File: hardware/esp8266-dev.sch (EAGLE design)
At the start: 14 parts, among them J1 AVR_SPI_PRG_6PTH, X2 PN61729-S

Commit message: generic little wire conversion complete
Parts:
- removed D1, D2: 3.6V, diode:ZENER-DIODEZD-5
- removed JP1: (no value), SparkFun:JUMPER-2PTH
- removed R4: 150, rcl:R-EU_0204/5
- removed X2: PN61729-S, con-berg:PN61729-S
- added C3: 100n, rcl:C-EU025-025X050
- added CON1: USBB-SOCKET, p.peter-connectors:USBB-SOCKET
- added ESP8266: (no value), pinhead:PINHD-2X4
- added F1: PTCPTH, SparkFun:PTCPTH
- added IC1: TBD, v-reg:78LXX
- added R5: 150, rcl:R-EU_0204/7
- added SJ1: (no value), jumper:SJ
- added SW1: (no value), p.peter-passives:SWITCH-DEFAULT_OFF-DEFAULT
- added UART-AVR, UART-ESP: UART-6_PIN, p.peter-connectors:UART-6_PIN
- C1, C2: device rcl:C-EU050-025X075 -> rcl:C-EU025-025X050
- R1, R2, R3: device rcl:R-EU_0204/5 -> rcl:R-EU_0204/7
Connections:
- removed net D-: D2.C, R2.1, R3.1, X2.1
- removed net VCC: C1.2, C2.2, JP1.1, R3.2, R4.2, UC.VCC, X2.4
- new net +3V3: C1.2, C3.2, IC1.OUT, LED1.A, SJ1.2, UART-AVR.VCC, UART-ESP.VCC, UC.VCC
- new net +5V: C2.2, F1.1, IC1.IN, R3.2
- new net N$4: CON1.VBUS, F1.2
- new net N$5: CON1.D-, R2.1, R3.1
- new net N$6: UART-AVR.TX, UART-ESP.TX
- new net N$7: UART-AVR.RX, UART-ESP.RX
- net D+: now also CON1.D+; no longer D1.C, X2.2
- net GND: now also C3.1, CON1.GND, IC1.GND, R5.1, UART-AVR.GND, UART-ESP.GND; no longer D1.A, D2.A, LED1.C, X2.3
- net N$3: now also LED1.C, R5.2; no longer LED1.A, R4.1
- net VCC_HEADER: now also SJ1.1; no longer JP1.2
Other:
- moved on the sheet: C2, LED1, R1, R2, R3

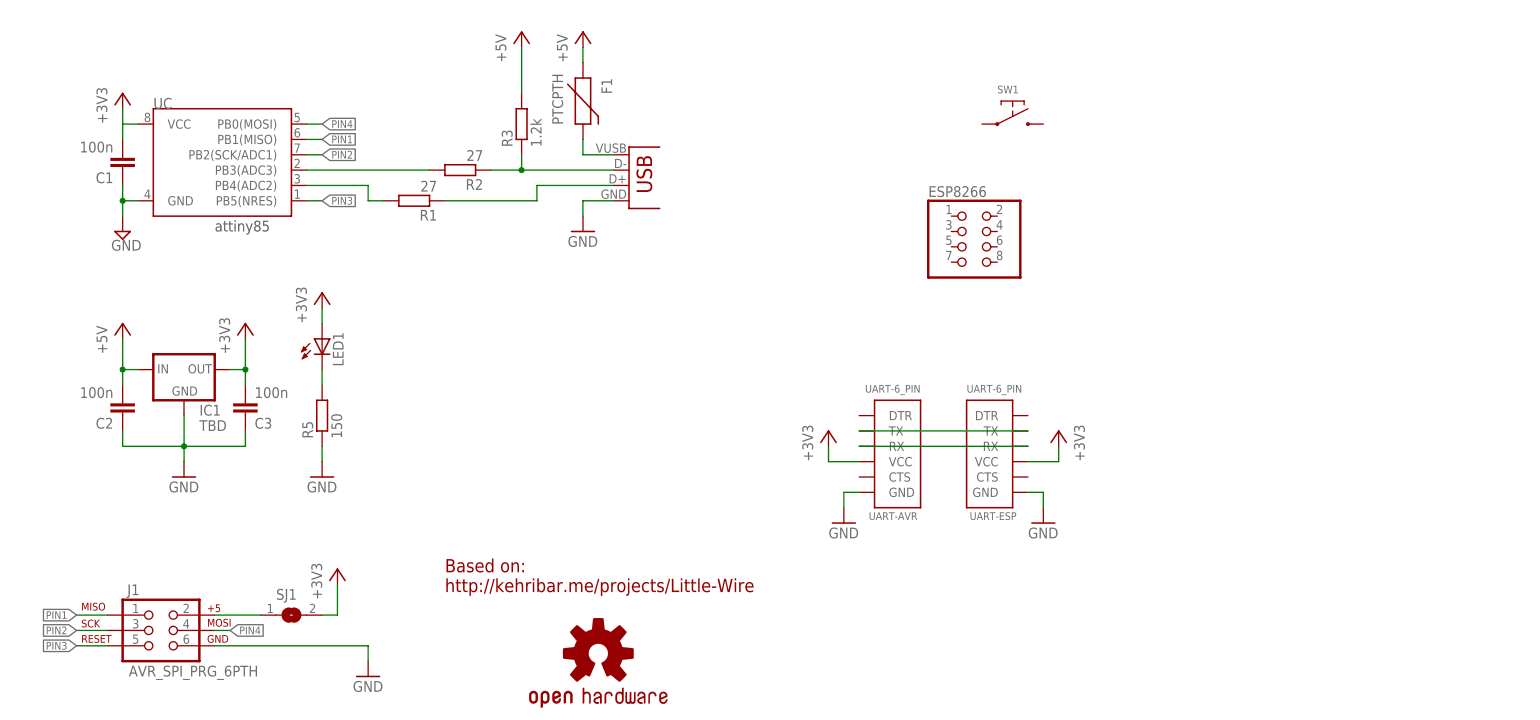
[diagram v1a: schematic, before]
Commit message: Added ESP sub board with proto area
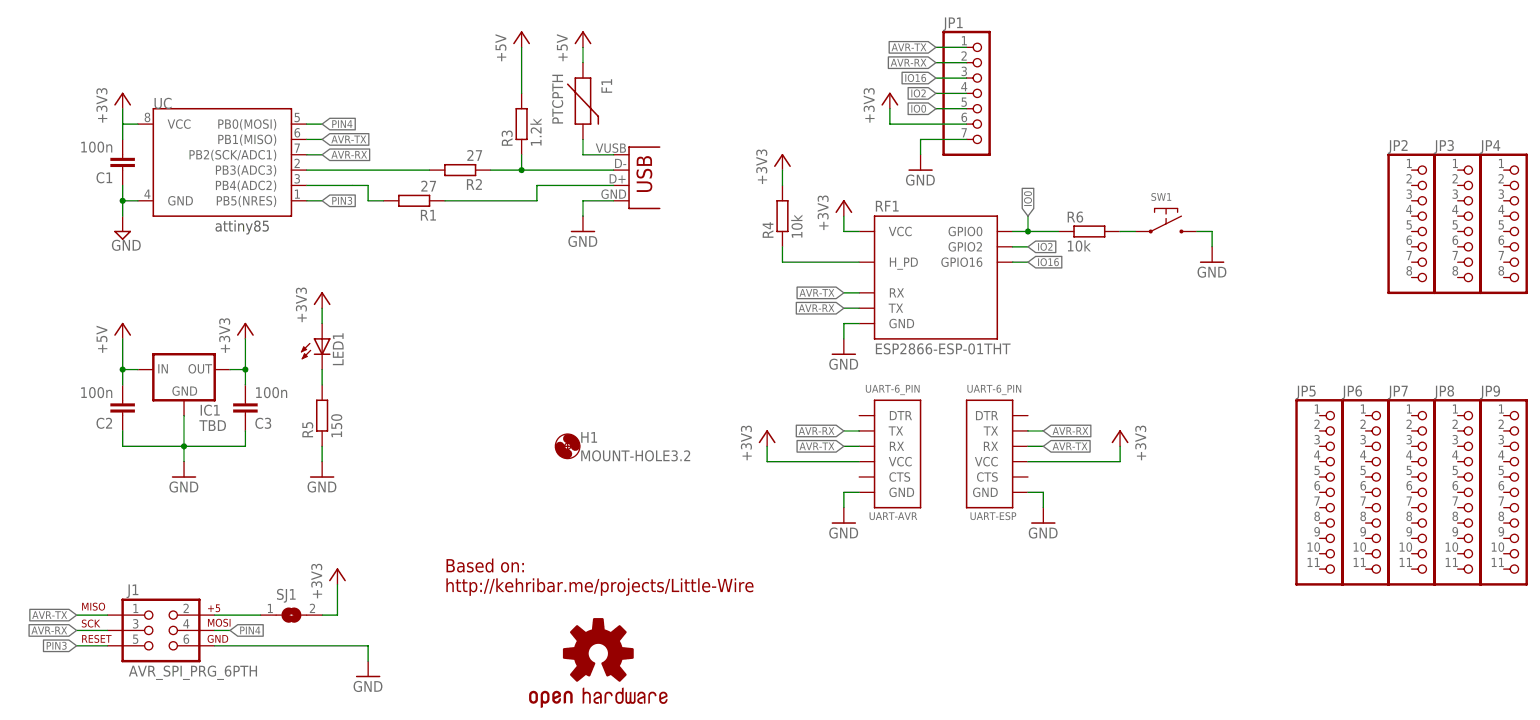
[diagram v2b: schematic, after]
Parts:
- removed ESP8266: (no value), pinhead:PINHD-2X4
- added H1: MOUNT-HOLE3.2, holes:MOUNT-HOLE3.2
- added JP1: (no value), pinhead:PINHD-1X7
- added JP2, JP3, JP4: (no value), pinhead:PINHD-1X8
- added JP5, JP6, JP7, JP8, JP9: (no value), pinhead:PINHD-1X11
- added R4, R6: 10k, rcl:R-EU_0204/7
- added RF1: ESP2866-ESP-01THT, p.peter-periphery:ESP2866-ESP-01THT
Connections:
- removed net N$7: UART-AVR.RX, UART-ESP.RX
- removed net PIN1: J1.1, UC.PB1(MISO)
- removed net PIN2: J1.3, UC.PB2(SCK/ADC1)
- new net AVR-RX: J1.3, JP1.2, RF1.TX, UART-AVR.TX, UART-ESP.TX, UC.PB2(SCK/ADC1)
- new net AVR-TX: J1.1, JP1.1, RF1.RX, UART-AVR.RX, UART-ESP.RX, UC.PB1(MISO)
- new net IO0: JP1.5, R6.1, RF1.GPIO0
- new net IO16: JP1.3, RF1.GPIO16
- new net IO2: JP1.4, RF1.GPIO2
- new net N$8: R6.2, SW1.P$1
- net +3V3: now also JP1.6, R4.2, RF1.VCC
- net GND: now also JP1.7, RF1.GND, SW1.P$2
- net N$6: now also R4.1, RF1.H_PD; no longer UART-AVR.TX, UART-ESP.TX
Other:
- moved on the sheet: SW1

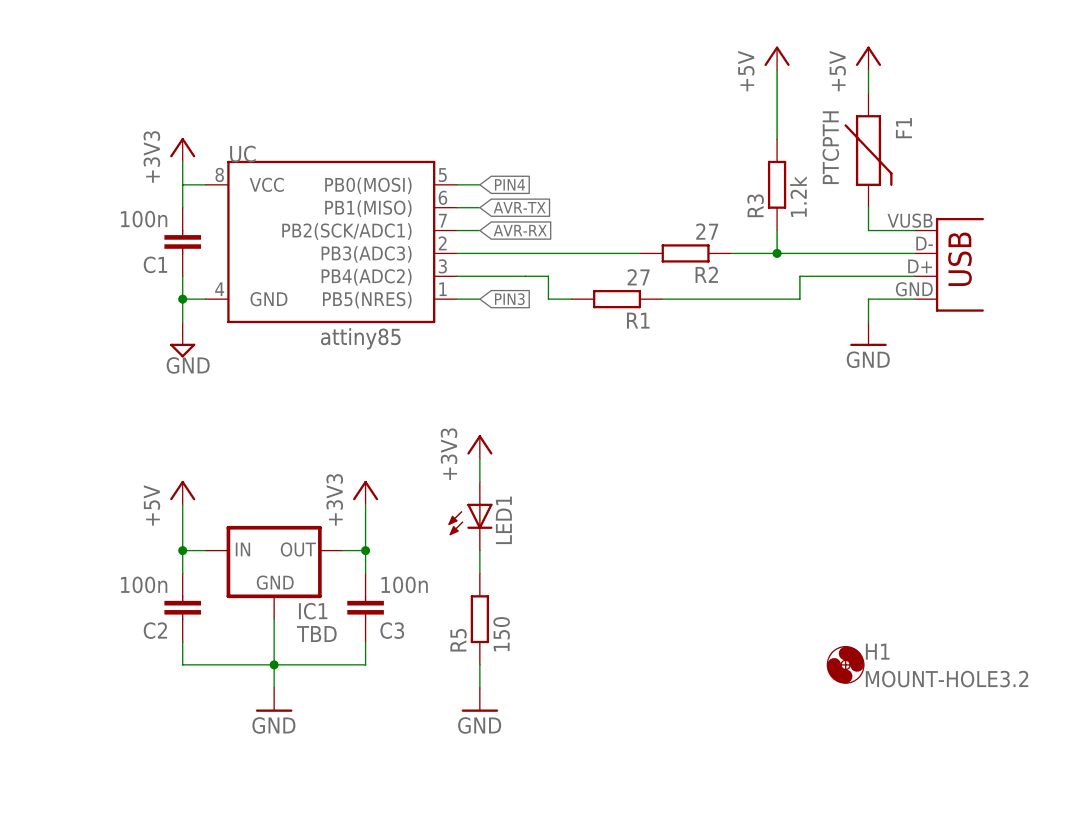
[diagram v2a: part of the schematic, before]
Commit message: changed regulator to 500m suitable version and fuse to smaller footprint
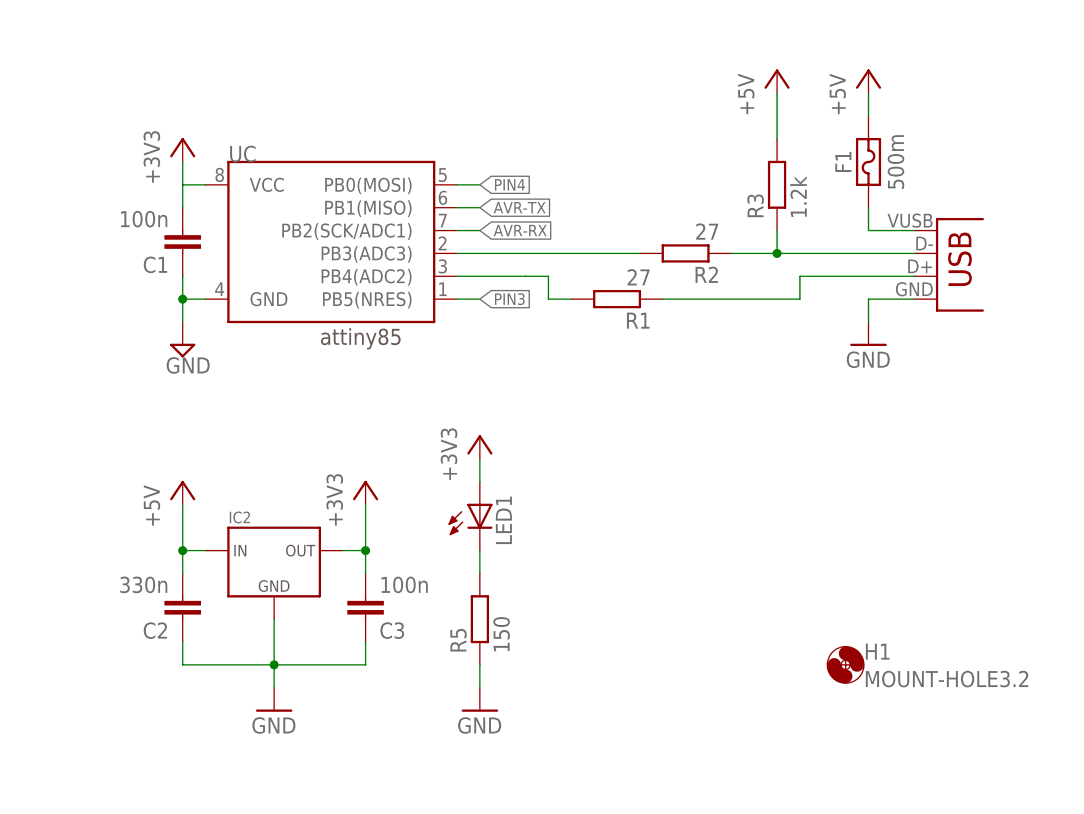
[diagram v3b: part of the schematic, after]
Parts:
- removed IC1: TBD, v-reg:78LXX
- added IC2: (no value), p.peter-regulators:REGULATOR-UA78M33TO220
- C2: value 100n -> 330n
- F1: value PTCPTH -> 500m; device SparkFun:PTCPTH -> p.peter-regulators:FUSETHT-5.1
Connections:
- net +3V3: now also IC2.OUT; no longer IC1.OUT
- net +5V: now also F1.P$2, IC2.IN; no longer F1.1, IC1.IN
- net GND: now also IC2.GND; no longer IC1.GND
- net N$4: now also F1.P$1; no longer F1.2
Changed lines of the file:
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@@
 <layer number="108" name="centerline" color="7" fill="1" visible="no" active="yes"/>
 <layer number="109" name="ref-old" color="11" fill="1" visible="no" active="yes"/>
+<layer number="110" name="fp0" color="7" fill="1" visible="no" active="yes"/>
 <layer number="116" name="Patch_BOT" color="9" fill="4" visible="yes" active="yes"/>
 <layer number="121" name="_tsilk" color="7" fill="1" visible="yes" active="yes"/>
 <layer number="122" name="_bsilk" color="7" fill="1" visible="yes" active="yes"/>
+<layer number="123" name="tTestmark" color="7" fill="1" visible="no" active="yes"/>
+<layer number="124" name="bTestmark" color="7" fill="1" visible="no" active="yes"/>
 <layer number="125" name="_tNames" color="7" fill="1" visible="yes" active="yes"/>
 <layer number="131" name="prix" color="7" fill="1" visible="no" active="yes"/>
@@
 <part name="U$1" library="SparkFun" deviceset="OSHW-LOGO" device="S"/>
 <part name="LED1" library="led" deviceset="LED" device="3MM"/>
-<part name="IC1" library="v-reg" deviceset="78LXX" device="" value="TBD"/>
 <part name="P+1" library="supply1" deviceset="+5V" device=""/>
 <part name="+3V1" library="supply1" deviceset="+3V3" device=""/>
@@
 <part name="+3V4" library="supply1" deviceset="+3V3" device=""/>
 <part name="P+3" library="supply1" deviceset="+5V" device=""/>
-<part name="C2" library="rcl" deviceset="C-EU" device="025-025X050" value="100n"/>
+<part name="C2" library="rcl" deviceset="C-EU" device="025-025X050" value="330n"/>
 <part name="C3" library="rcl" deviceset="C-EU" device="025-025X050" value="100n"/>
 <part name="UART-AVR" library="p.peter-connectors" deviceset="UART-6_PIN" device=""/>
@@
 <part name="+3V6" library="supply1" deviceset="+3V3" device=""/>
 <part name="SW1" library="p.peter-passives" deviceset="SWITCH-DEFAULT_OFF" device="-DEFAULT"/>
-<part name="F1" library="SparkFun" deviceset="PTC" device="PTH"/>
 <part name="SJ1" library="jumper" deviceset="SJ" device=""/>
 <part name="CON1" library="p.peter-connectors" deviceset="USB" device="B-SOCKET"/>
@@
 <part name="GND9" library="supply1" deviceset="GND" device=""/>
 <part name="+3V9" library="supply1" deviceset="+3V3" device=""/>
+<part name="IC2" library="p.peter-regulators" deviceset="REGULATOR-UA78M33" device="TO220"/>
+<part name="F1" library="p.peter-regulators" deviceset="FUSE" device="THT-5.1" value="500m"/>
 </parts>
 <sheets>
@@
 <instance part="U$1" gate="G$1" x="111.76" y="13.97"/>
 <instance part="LED1" gate="G$1" x="66.04" y="66.04"/>
-<instance part="IC1" gate="1" x="43.18" y="60.96"/>
-<instance part="P+1" gate="1" x="109.22" y="116.84"/>
+<instance part="P+1" gate="1" x="109.22" y="114.3"/>
 <instance part="+3V1" gate="G$1" x="53.34" y="68.58"/>
 <instance part="GND1" gate="1" x="43.18" y="43.18"/>
@@
 <instance part="+3V2" gate="G$1" x="66.04" y="73.66"/>
 <instance part="R5" gate="G$1" x="66.04" y="53.34" rot="R90"/>
-<instance part="P+2" gate="1" x="99.06" y="116.84"/>
+<instance part="P+2" gate="1" x="99.06" y="114.3"/>
 <instance part="GND3" gate="1" x="109.22" y="83.82"/>
 <instance part="GND4" gate="1" x="73.66" y="10.16"/>
@@
 <instance part="+3V6" gate="G$1" x="198.12" y="50.8" rot="MR0"/>
 <instance part="SW1" gate="S$1" x="205.74" y="83.82"/>
-<instance part="F1" gate="G$1" x="109.22" y="106.68" rot="R270"/>
 <instance part="SJ1" gate="1" x="60.96" y="20.32"/>
 <instance part="CON1" gate="G$1" x="116.84" y="91.44" rot="MR0"/>
@@
 <instance part="GND9" gate="1" x="165.1" y="93.98"/>
 <instance part="+3V9" gate="G$1" x="160.02" y="106.68"/>
+<instance part="IC2" gate="G$1" x="43.18" y="60.96"/>
+<instance part="F1" gate="G$1" x="109.22" y="104.14" rot="R90"/>
 </instances>
 <busses>
@@
 </segment>
 <segment>
-<pinref part="IC1" gate="1" pin="GND"/>
 <pinref part="GND1" gate="1" pin="GND"/>
 <wire x1="43.18" y1="45.72" x2="43.18" y2="48.26" width="0.1524" layer="91"/>
@@
 <wire x1="33.02" y1="48.26" x2="43.18" y2="48.26" width="0.1524" layer="91"/>
 <junction x="43.18" y="48.26"/>
+<pinref part="IC2" gate="G$1" pin="GND"/>
 </segment>
 <segment>
@@
 </segment>
 <segment>
-<pinref part="IC1" gate="1" pin="OUT"/>
 <pinref part="+3V1" gate="G$1" pin="+3V3"/>
 <wire x1="53.34" y1="66.04" x2="53.34" y2="60.96" width="0.1524" layer="91"/>
@@
 <wire x1="53.34" y1="58.42" x2="53.34" y2="60.96" width="0.1524" layer="91"/>
 <junction x="53.34" y="60.96"/>
+<pinref part="IC2" gate="G$1" pin="OUT"/>
 </segment>
 <segment>
@@
 <net name="+5V" class="0">
 <segment>
-<wire x1="99.06" y1="106.68" x2="99.06" y2="114.3" width="0.1524" layer="91"/>
+<wire x1="99.06" y1="106.68" x2="99.06" y2="111.76" width="0.1524" layer="91"/>
 <pinref part="R3" gate="G$1" pin="2"/>
 <pinref part="P+2" gate="1" pin="+5V"/>
 </segment>
 <segment>
-<pinref part="IC1" gate="1" pin="IN"/>
 <pinref part="P+3" gate="1" pin="+5V"/>
 <wire x1="33.02" y1="66.04" x2="33.02" y2="60.96" width="0.1524" layer="91"/>
@@
 <wire x1="33.02" y1="58.42" x2="33.02" y2="60.96" width="0.1524" layer="91"/>
 <junction x="33.02" y="60.96"/>
-</segment>
-<segment>
-<pinref part="F1" gate="G$1" pin="1"/>
+<pinref part="IC2" gate="G$1" pin="IN"/>
+</segment>
+<segment>
 <pinref part="P+1" gate="1" pin="+5V"/>
-<wire x1="109.22" y1="111.76" x2="109.22" y2="114.3" width="0.1524" layer="91"/>
+<wire x1="109.22" y1="109.22" x2="109.22" y2="111.76" width="0.1524" layer="91"/>
+<pinref part="F1" gate="G$1" pin="P$2"/>
 </segment>
 </net>
@@
 <segment>
 <pinref part="CON1" gate="G$1" pin="VBUS"/>
-<pinref part="F1" gate="G$1" pin="2"/>
 <wire x1="114.3" y1="96.52" x2="109.22" y2="96.52" width="0.1524" layer="91"/>
 <wire x1="109.22" y1="96.52" x2="109.22" y2="99.06" width="0.1524" layer="91"/>
-</segment>
-</net>
+<pinref part="F1" gate="G$1" pin="P$1"/>
+</segment>
+</net>
